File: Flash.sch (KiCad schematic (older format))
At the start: 1 part, among them U10 W25Q128JVS

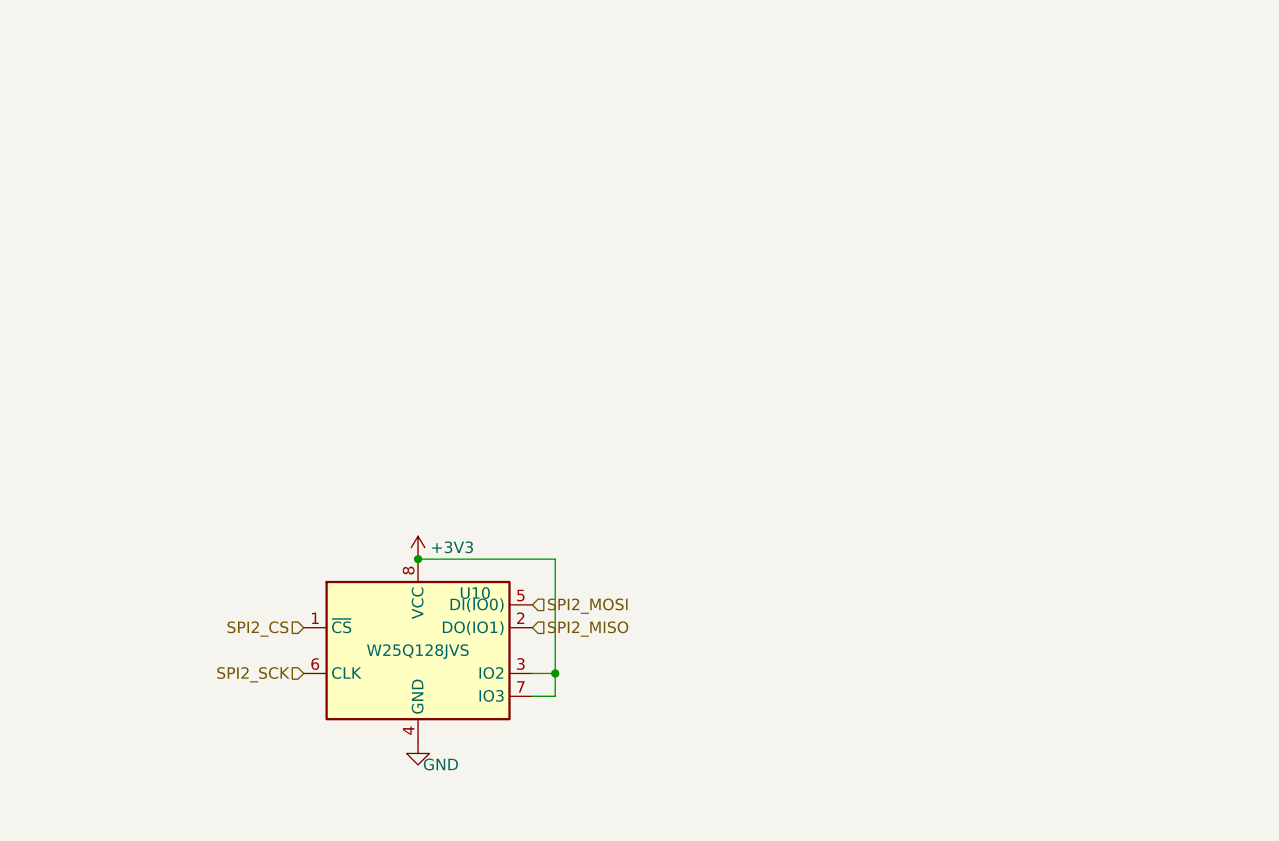
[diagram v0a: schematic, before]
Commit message: Updated the schematics to include pictures
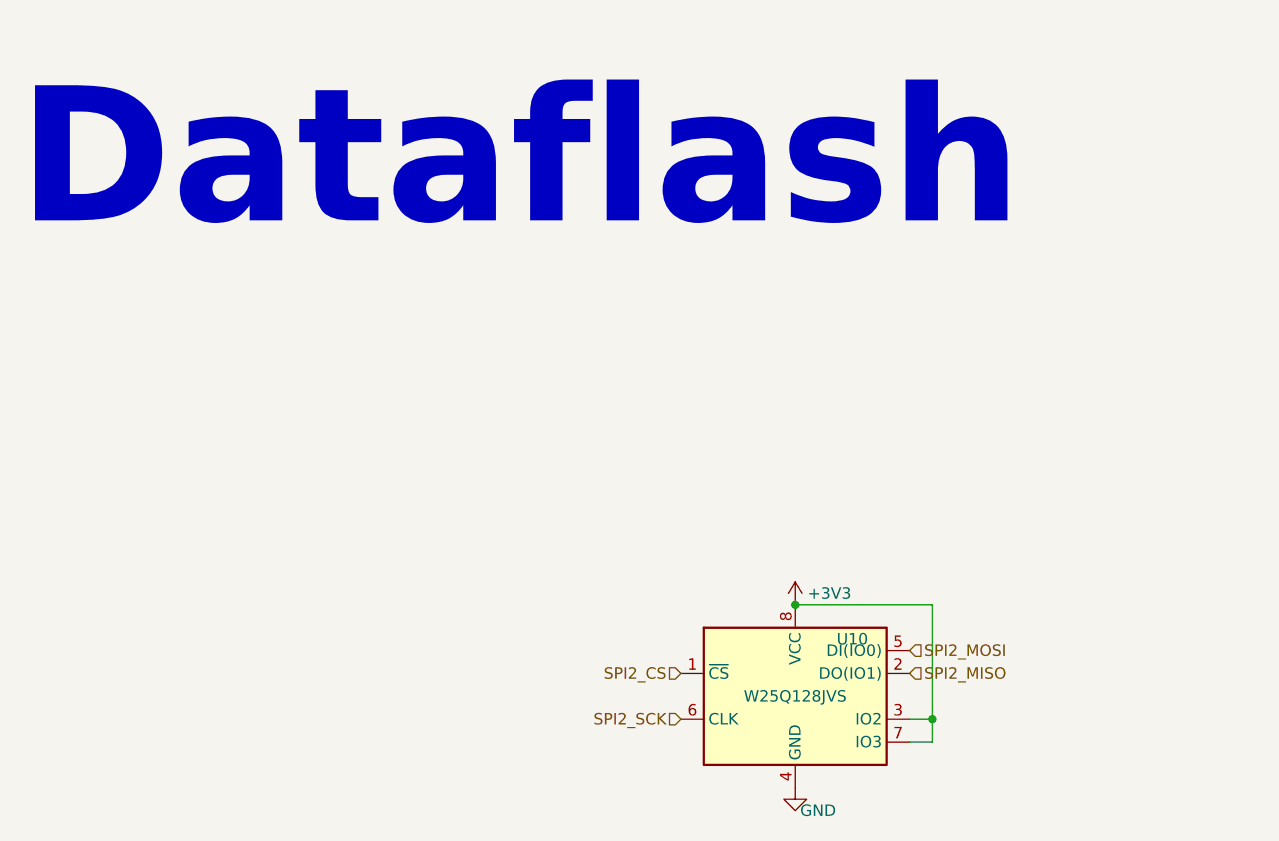
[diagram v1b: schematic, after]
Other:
- note added: "Dataflash"
- moved on the sheet: U10
